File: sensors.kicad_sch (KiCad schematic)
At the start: 21 parts, among them U11 BMP280, U12 MMC5633NJL, U16 Si7020-A20, U17 TXB0108PW, U3 IIM-42652, U4 QMI8610, U9 PCA9306DC1

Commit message: MOS管修改为GSD, 添加芯片附近滤波电容、上拉电阻等，调整模块间布局，改正AHT20封装，电解电容替换成1210 MLCC
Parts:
- removed U16: Si7020-A20, Package_DFN_QFN:DFN-6-1EP_3x3mm_P1mm_EP1.5x2.4mm, symbol Sensor_Humidity:Si7020-A20
- added C33: 2.2uf, Capacitor_SMD:C_0603_1608Metric, symbol Device:C_Small
- added C34: 10uf, Capacitor_SMD:C_0603_1608Metric, symbol Device:C
- added C35: 0.1uf, Capacitor_SMD:C_0402_1005Metric, symbol Device:C_Small
- added R32: R, Resistor_SMD:R_0603_1608Metric, symbol Device:R
- added U5: AHT20, Library:DFN-6_3x3mm_P1.0mm_AHT2x_AHT30, symbol New_Library:AHT2x
- C10: value C_Small -> 10nF
- C11, C12, C15, C17, C18, C20, C21: value C_Small -> 100nF
- C19, C9: value C_Small -> 0.1uf
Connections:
- net +1V8: now also C33.2, C35.2
- net +3.3V: now also R32.1
- net GND: now also C33.1, C34.2, C35.1, U5.5 (GND)
- net SCL: now also U5.3 (SCL)
- net SDA: now also U5.4 (SDA)
- new net: U5.1 (NC), U5.6 (NC)
- new net: C34.1, R32.2, U5.2 (VDD)
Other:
- moved on the sheet: C10

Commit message: 连接大多数布线，做一些调整，添加覆铜
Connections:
- net +1V8: now also U11.2 (CSB)
- net SCL1V8: now also U11.4 (SCK)
- net SDA1V8: now also U11.3 (SDI)
- net SPISen_CS_QMI_1V8: now also U17.4 (A3); no longer U17.1 (A1)
- net SPISen_CS_TDK_1V8: now also U17.8 (A7); no longer U17.3 (A2)
- net SPISen_MISO_1V8: now also U17.6 (A5); no longer U11.5 (SDO), U17.7 (A6)
- net SPISen_MOSI_1V8: now also U17.7 (A6); no longer U11.3 (SDI), U17.5 (A4)
- net SPISen_SCLK_1V8: now also U17.5 (A4); no longer U11.4 (SCK), U17.6 (A5)
- net TDK_INT2_1V8: now also U17.9 (A8); no longer U17.8 (A7)
- net TDK_INT2_3V3: now also U17.12 (B8); no longer U17.13 (B7)
- removed net SPISen_CS_BMP_1V8: U11.2 (CSB), U17.4 (A3)
- net SPISen_CS_BMP_3V3 renamed CS_QMI_3V3
- net SPISen_CS_QMI_3V3: no longer names the net of U17.20 (B1)
- net SPISen_CS_TDK_3V3: no longer names the net of U17.18 (B2)
- net SPISen_MISO_3V3 renamed MOSI_3V3
- net SPISen_MOSI_3V3 renamed SCLK_3V3
- net SPISen_SCLK_3V3 renamed MISO_3V3
- new net CS_TDK_3V3: U17.13 (B7)
- no-connect marks 2 -> 3
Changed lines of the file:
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@@
+	)
+	(junction
+		(at 158.75 104.14)
+		(diameter 0)
+		(color 0 0 0 0)
 	)
 	(junction
@@
 	)
 	(no_connect
+		(at 148.59 114.3)
+	)
+	(no_connect
 		(at 146.05 44.45)
 	)
@@
 	(wire
 		(pts
-			(xy 147.32 116.84) (xy 148.59 116.84)
-		)
-		(stroke
-			(width 0)
-			(type default)
-		)
-	)
-	(wire
-		(pts
 			(xy 243.84 76.2) (xy 245.11 76.2)
 		)
@@
 	(wire
 		(pts
-			(xy 147.32 114.3) (xy 148.59 114.3)
-		)
-		(stroke
-			(width 0)
-			(type default)
-		)
-	)
-	(wire
-		(pts
 			(xy 115.57 113.03) (xy 115.57 116.84)
 		)
@@
 	(wire
 		(pts
+			(xy 158.75 116.84) (xy 158.75 104.14)
+		)
+		(stroke
+			(width 0)
+			(type default)
+		)
+	)
+	(wire
+		(pts
 			(xy 166.37 115.57) (xy 166.37 123.19)
 		)
@@
 	(wire
 		(pts
+			(xy 148.59 116.84) (xy 158.75 116.84)
+		)
+		(stroke
+			(width 0)
+			(type default)
+		)
+	)
+	(wire
+		(pts
 			(xy 220.98 78.74) (xy 223.52 78.74)
 		)
@@
 		)
 	)
-	(label "SPISen_MOSI_3V3"
-		(at 245.11 68.58 0)
-		(fields_autoplaced yes)
-		(effects
-			(font
-				(size 1.27 1.27)
-			)
-			(justify left bottom)
+	(label "SDA1V8"
+		(at 147.32 111.76 180)
+		(fields_autoplaced yes)
+		(effects
+			(font
+				(size 1.27 1.27)
+			)
+			(justify right bottom)
 		)
 	)
 	(label "SPISen_MOSI_1V8"
-		(at 220.98 68.58 180)
+		(at 220.98 73.66 180)
 		(fields_autoplaced yes)
 		(effects
@@
 		)
 	)
-	(label "SPISen_CS_BMP_3V3"
-		(at 245.11 66.04 0)
-		(fields_autoplaced yes)
-		(effects
-			(font
-				(size 1.27 1.27)
-			)
-			(justify left bottom)
-		)
-	)
-	(label "SPISen_MOSI_1V8"
-		(at 147.32 111.76 180)
-		(fields_autoplaced yes)
-		(effects
-			(font
-				(size 1.27 1.27)
-			)
-			(justify right bottom)
-		)
-	)
 	(label "SDA1V8"
 		(at 46.99 80.01 180)
@@
 		)
 	)
-	(label "SPISen_CS_QMI_1V8"
-		(at 220.98 60.96 180)
-		(fields_autoplaced yes)
-		(effects
-			(font
-				(size 1.27 1.27)
-			)
-			(justify right bottom)
-		)
-	)
 	(label "QMI_INT2"
 		(at 172.72 40.64 0)
@@
 		)
 	)
-	(label "SPISen_CS_QMI_3V3"
-		(at 245.11 60.96 0)
-		(fields_autoplaced yes)
-		(effects
-			(font
-				(size 1.27 1.27)
-			)
-			(justify left bottom)
+	(label "SPISen_CS_TDK_1V8"
+		(at 220.98 76.2 180)
+		(fields_autoplaced yes)
+		(effects
+			(font
+				(size 1.27 1.27)
+			)
+			(justify right bottom)
 		)
 	)
@@
 		)
 	)
+	(label "SPISen_SCLK_1V8"
+		(at 220.98 68.58 180)
+		(fields_autoplaced yes)
+		(effects
+			(font
+				(size 1.27 1.27)
+			)
+			(justify right bottom)
+		)
+	)
 	(label "SPISen_MISO_1V8"
-		(at 147.32 114.3 180)
+		(at 220.98 71.12 180)
 		(fields_autoplaced yes)
 		(effects
@@
 		)
 	)
-	(label "SPISen_CS_TDK_1V8"
-		(at 220.98 63.5 180)
-		(fields_autoplaced yes)
-		(effects
-			(font
-				(size 1.27 1.27)
-			)
-			(justify right bottom)
-		)
-	)
 	(label "SPISen_MOSI_1V8"
 		(at 172.72 45.72 0)
@@
 		)
 	)
+	(label "TDK_INT2_1V8"
+		(at 220.98 78.74 180)
+		(fields_autoplaced yes)
+		(effects
+			(font
+				(size 1.27 1.27)
+			)
+			(justify right bottom)
+		)
+	)
 	(label "SCL1V8"
 		(at 46.99 77.47 180)
@@
 		)
 	)
-	(label "TDK_INT2_1V8"
-		(at 220.98 76.2 180)
-		(fields_autoplaced yes)
-		(effects
-			(font
-				(size 1.27 1.27)
-			)
-			(justify right bottom)
-		)
-	)
-	(label "SPISen_CS_BMP_1V8"
+	(label "SPISen_CS_QMI_1V8"
 		(at 220.98 66.04 180)
-		(fields_autoplaced yes)
-		(effects
-			(font
-				(size 1.27 1.27)
-			)
-			(justify right bottom)
-		)
-	)
-	(label "TDK_INT2_3V3"
-		(at 245.11 76.2 0)
-		(fields_autoplaced yes)
-		(effects
-			(font
-				(size 1.27 1.27)
-			)
-			(justify left bottom)
-		)
-	)
-	(label "SPISen_CS_BMP_1V8"
-		(at 147.32 116.84 180)
 		(fields_autoplaced yes)
 		(effects
@@
 		)
 	)
-	(label "SPISen_MISO_3V3"
-		(at 245.11 73.66 0)
-		(fields_autoplaced yes)
-		(effects
-			(font
-				(size 1.27 1.27)
-			)
-			(justify left bottom)
-		)
-	)
-	(label "SPISen_SCLK_1V8"
-		(at 220.98 71.12 180)
-		(fields_autoplaced yes)
-		(effects
-			(font
-				(size 1.27 1.27)
-			)
-			(justify right bottom)
-		)
-	)
 	(label "TDK_INT1"
 		(at 128.27 43.18 0)
@@
 		)
 	)
-	(label "SPISen_CS_TDK_3V3"
-		(at 245.11 63.5 0)
-		(fields_autoplaced yes)
-		(effects
-			(font
-				(size 1.27 1.27)
-			)
-			(justify left bottom)
-		)
-	)
-	(label "SPISen_MISO_1V8"
-		(at 220.98 73.66 180)
-		(fields_autoplaced yes)
-		(effects
-			(font
-				(size 1.27 1.27)
-			)
-			(justify right bottom)
-		)
-	)
 	(label "SDA"
 		(at 215.9 114.3 180)
@@
 	)
 	(label "SPISen_SCLK_1V8"
-		(at 147.32 109.22 180)
-		(fields_autoplaced yes)
-		(effects
-			(font
-				(size 1.27 1.27)
-			)
-			(justify right bottom)
-		)
-	)
-	(label "SPISen_SCLK_1V8"
 		(at 80.01 43.18 180)
 		(fields_autoplaced yes)
@@
 		)
 	)
-	(label "SPISen_SCLK_3V3"
-		(at 245.11 71.12 0)
-		(fields_autoplaced yes)
-		(effects
-			(font
-				(size 1.27 1.27)
-			)
-			(justify left bottom)
+	(label "SCL1V8"
+		(at 147.32 109.22 180)
+		(fields_autoplaced yes)
+		(effects
+			(font
+				(size 1.27 1.27)
+			)
+			(justify right bottom)
 		)
 	)
@@
 		(fields_autoplaced yes)
 		(effects
+			(font
+				(size 1.27 1.27)
+			)
+			(justify left)
+		)
+	)
+	(hierarchical_label "MISO_3V3"
+		(shape output)
+		(at 245.11 71.12 0)
+		(fields_autoplaced yes)
+		(effects
+			(font
+				(size 1.27 1.27)
+			)
+			(justify left)
+		)
+	)
+	(hierarchical_label "MOSI_3V3"
+		(shape input)
+		(at 245.11 73.66 0)
+		(fields_autoplaced yes)
+		(effects
+			(font
+				(size 1.27 1.27)
+			)
+			(justify left)
+		)
+	)
+	(hierarchical_label "CS_TDK_3V3"
+		(shape input)
+		(at 245.11 76.2 0)
+		(fields_autoplaced yes)
+		(effects
+			(font
+				(size 1.27 1.27)
+			)
+			(justify left)
+		)
+	)
+	(hierarchical_label "TDK_INT2_3V3"
+		(shape bidirectional)
+		(at 245.11 78.74 0)
+		(fields_autoplaced yes)
+		(effects
+			(font
+				(size 1.27 1.27)
+			)
+			(justify left)
+		)
+	)
+	(hierarchical_label "CS_QMI_3V3"
+		(shape input)
+		(at 245.11 66.04 0)
+		(fields_autoplaced yes)
+		(effects
+			(font
+				(size 1.27 1.27)
+			)
+			(justify left)
+		)
+	)
+	(hierarchical_label "SCLK_3V3"
+		(shape input)
+		(at 245.11 68.58 0)
+		(fields_autoplaced yes)
+		(effects

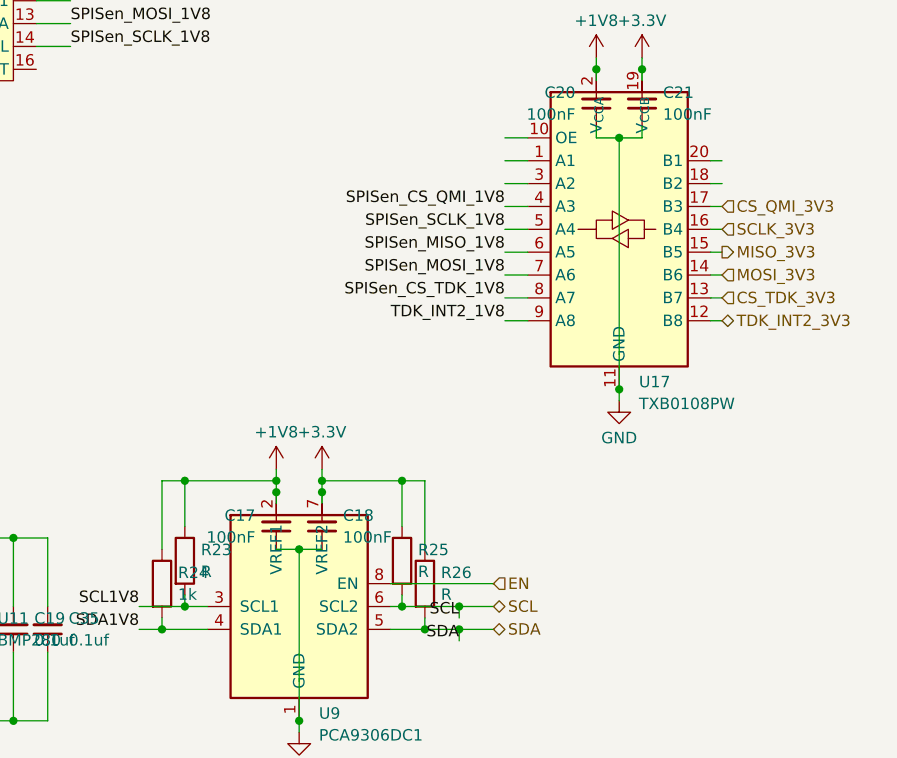
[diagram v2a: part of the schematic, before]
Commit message: 移除第二个74HC595，SGM2033-1.8改成一直开启，按PCA9306数据手册修改供电
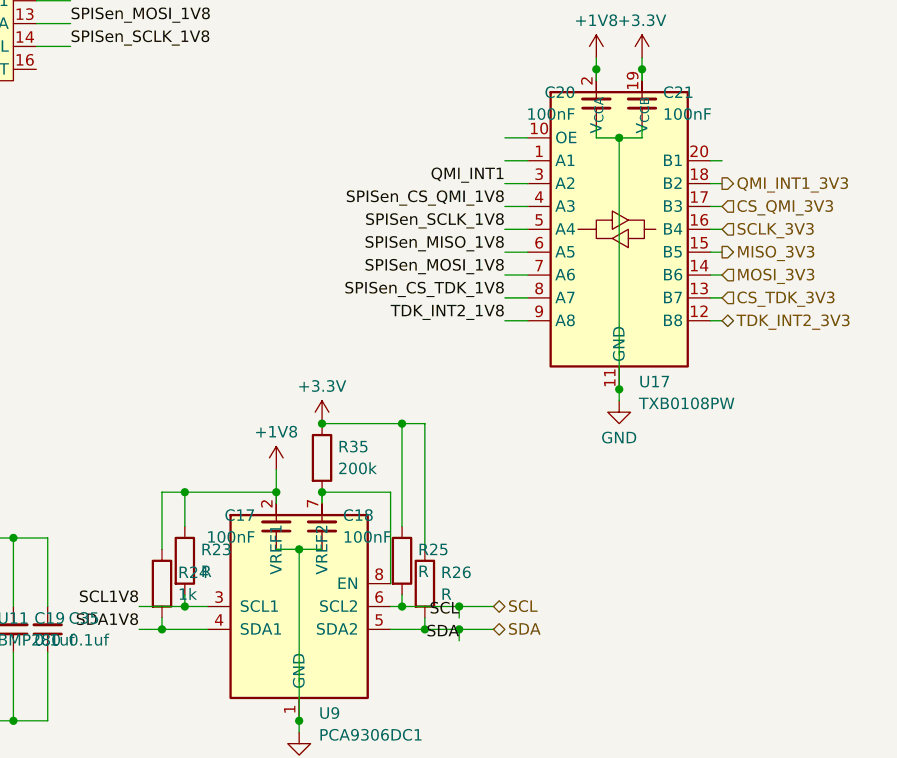
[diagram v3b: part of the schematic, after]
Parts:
- added R35: 200k, Resistor_SMD:R_0402_1005Metric, symbol Device:R
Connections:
- net +3.3V: now also R35.1; no longer C18.2, U9.7 (VREF2)
- net QMI_INT1: now also U17.3 (A2)
- net QMI_INT1_3V3: now reaches U17.18 (B2)
- net EN: no longer names the net of U9.8 (EN)
- net EN: now also C18.2, U9.7 (VREF2), R35.2
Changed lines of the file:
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@@
 	)
 	(junction
-		(at 185.42 96.52)
+		(at 209.55 90.17)
 		(diameter 0)
 		(color 0 0 0 0)
@@
 	)
 	(junction
-		(at 195.58 96.52)
-		(diameter 0)
-		(color 0 0 0 0)
-	)
-	(junction
 		(at 97.79 24.13)
 		(diameter 0)
@@
 	)
 	(junction
-		(at 200.66 96.52)
-		(diameter 0)
-		(color 0 0 0 0)
-	)
-	(junction
 		(at 212.09 113.03)
 		(diameter 0)
@@
 	)
 	(junction
+		(at 185.42 97.79)
+		(diameter 0)
+		(color 0 0 0 0)
+	)
+	(junction
 		(at 161.29 102.87)
 		(diameter 0)
@@
 	)
 	(junction
+		(at 200.66 90.17)
+		(diameter 0)
+		(color 0 0 0 0)
+	)
+	(junction
 		(at 161.29 123.19)
 		(diameter 0)
@@
 	)
 	(junction
-		(at 209.55 96.52)
-		(diameter 0)
-		(color 0 0 0 0)
-	)
-	(junction
 		(at 215.9 110.49)
 		(diameter 0)
@@
 	(wire
 		(pts
-			(xy 195.58 97.79) (xy 195.58 96.52)
-		)
-		(stroke
-			(width 0)
-			(type default)
-		)
-	)
-	(wire
-		(pts
 			(xy 104.14 29.21) (xy 104.14 30.48)
 		)
@@
 	(wire
 		(pts
-			(xy 195.58 95.25) (xy 195.58 96.52)
+			(xy 200.66 97.79) (xy 200.66 99.06)
 		)
 		(stroke
@@
 	(wire
 		(pts
-			(xy 212.09 96.52) (xy 209.55 96.52)
+			(xy 212.09 90.17) (xy 209.55 90.17)
 		)
 		(stroke
@@
 	(wire
 		(pts
-			(xy 200.66 96.52) (xy 209.55 96.52)
+			(xy 200.66 90.17) (xy 209.55 90.17)
 		)
 		(stroke
@@
 	(wire
 		(pts
-			(xy 182.88 96.52) (xy 185.42 96.52)
+			(xy 182.88 97.79) (xy 185.42 97.79)
 		)
 		(stroke
@@
 	(wire
 		(pts
-			(xy 170.18 110.49) (xy 170.18 102.87)
+			(xy 208.28 97.79) (xy 208.28 107.95)
 		)
 		(stroke
@@
 	(wire
 		(pts
-			(xy 115.57 113.03) (xy 115.57 116.84)
+			(xy 195.58 95.25) (xy 195.58 97.79)
 		)
 		(stroke
@@
 	(wire
 		(pts
-			(xy 71.12 72.39) (xy 58.42 72.39)
+			(xy 170.18 110.49) (xy 170.18 102.87)
 		)
 		(stroke
@@
 	(wire
 		(pts
-			(xy 158.75 104.14) (xy 158.75 102.87)
+			(xy 115.57 113.03) (xy 115.57 116.84)
 		)
 		(stroke
@@
 	(wire
 		(pts
-			(xy 209.55 101.6) (xy 209.55 96.52)
+			(xy 71.12 72.39) (xy 58.42 72.39)
 		)
 		(stroke
@@
 	(wire
 		(pts
-			(xy 166.37 110.49) (xy 166.37 102.87)
+			(xy 158.75 104.14) (xy 158.75 102.87)
 		)
 		(stroke
@@
 	(wire
 		(pts
-			(xy 115.57 101.6) (xy 107.95 101.6)
+			(xy 209.55 90.17) (xy 209.55 101.6)
 		)
 		(stroke
@@
 	(wire
 		(pts
-			(xy 158.75 102.87) (xy 160.02 102.87)
+			(xy 166.37 110.49) (xy 166.37 102.87)
 		)
 		(stroke
@@
 	(wire
 		(pts
-			(xy 198.12 123.19) (xy 198.12 124.46)
+			(xy 115.57 101.6) (xy 107.95 101.6)
 		)
 		(stroke
@@
 	(wire
 		(pts
-			(xy 200.66 95.25) (xy 200.66 96.52)
+			(xy 158.75 102.87) (xy 160.02 102.87)
 		)
 		(stroke
@@
 	(wire
 		(pts
-			(xy 46.99 80.01) (xy 48.26 80.01)
+			(xy 198.12 123.19) (xy 198.12 124.46)
 		)
 		(stroke
@@
 	(wire
 		(pts
-			(xy 212.09 104.14) (xy 212.09 96.52)
+			(xy 46.99 80.01) (xy 48.26 80.01)
 		)
 		(stroke
@@
 	(wire
 		(pts
-			(xy 200.66 99.06) (xy 200.66 97.79)
+			(xy 212.09 90.17) (xy 212.09 104.14)
 		)
 		(stroke
@@
 	(wire
 		(pts
-			(xy 200.66 96.52) (xy 200.66 97.79)
-		)
-		(stroke
-			(width 0)
-			(type default)
-		)
-	)
-	(wire
-		(pts
 			(xy 212.09 111.76) (xy 212.09 113.03)
 		)
@@
 	(wire
 		(pts
-			(xy 182.88 104.14) (xy 182.88 96.52)
+			(xy 182.88 104.14) (xy 182.88 97.79)
 		)
 		(stroke
@@
 	(wire
 		(pts
-			(xy 185.42 101.6) (xy 185.42 96.52)
+			(xy 185.42 101.6) (xy 185.42 97.79)
 		)
 		(stroke
@@
 	(wire
 		(pts
-			(xy 185.42 96.52) (xy 195.58 96.52)
+			(xy 185.42 97.79) (xy 195.58 97.79)
 		)
 		(stroke
@@
 	(wire
 		(pts
-			(xy 208.28 107.95) (xy 219.71 107.95)
+			(xy 200.66 97.79) (xy 208.28 97.79)
 		)
 		(stroke
@@
 		)
 	)
+	(label "QMI_INT1"
+		(at 220.98 63.5 180)
+		(fields_autoplaced yes)
+		(effects
+			(font
+				(size 1.27 1.27)
+			)
+			(justify right bottom)
+		)
+	)
 	(label "TDK_INT2_1V8"
 		(at 220.98 78.74 180)
@@
 		)
 	)
-	(hierarchical_label "EN"
-		(shape input)
-		(at 219.71 107.95 0)
+	(hierarchical_label "QMI_INT1_3V3"
+		(shape output)
+		(at 245.11 63.5 0)
 		(fields_autoplaced yes)
 		(effects
@@
 	)
 	(symbol
+		(lib_id "Device:R")
+		(at 200.66 93.98 0)
+		(unit 1)
+		(exclude_from_sim no)
+		(in_bom yes)
+		(on_board yes)
+		(dnp no)
+		(fields_autoplaced yes)
+		(property "Reference" "R35"
+			(at 202.438 92.7678 0)
+			(effects
+				(font
+					(size 1.27 1.27)
+				)
+				(justify left)
+			)
+		)
+		(property "Value" "200k"
+			(at 202.438 95.1921 0)
+			(effects
+				(font
+					(size 1.27 1.27)
+				)
+				(justify left)
+			)
+		)
+		(property "Footprint" "Resistor_SMD:R_0402_1005Metric"
+			(at 198.882 93.98 90)
+			(effects
+				(font
+					(size 1.27 1.27)
+				)
+				(hide yes)
+			)
+		)
+		(property "Datasheet" "~"
+			(at 200.66 93.98 0)
+			(effects
+				(font
+					(size 1.27 1.27)
+				)
+				(hide yes)
+			)
+		)
+		(property "Description" "Resistor"
+			(at 200.66 93.98 0)
+			(effects
+				(font
+					(size 1.27 1.27)
+				)
+				(hide yes)
+			)
+		)
+		(property "Sim.Type" ""
+			(at 200.66 93.98 0)
+			(effects
+				(font
+					(size 1.27 1.27)
+				)
+				(hide yes)
+			)
+		)
+		(pin "2"
+		)
+		(pin "1"
+		)
+		(instances
+			(project "bicycle_board"
+				(path "/a369956d-4c9f-46c3-810f-e3e9616ab1a2/490df38e-4ea0-4947-96c5-2fbeb0d565d2"
+					(reference "R35")
+					(unit 1)
+				)
+			)
+		)
+	)
+	(symbol
 		(lib_id "power:GND")
 		(at 233.68 87.63 0)
@@
 	(symbol
 		(lib_id "power:+3.3V")
-		(at 200.66 95.25 0)
+		(at 200.66 90.17 0)
 		(unit 1)
 		(exclude_from_sim no)
@@
 		(fields_autoplaced yes)
 		(property "Reference" "#PWR037"
-			(at 200.66 99.06 0)
+			(at 200.66 93.98 0)
 			(effects
 				(font
@@
 		)
 		(property "Value" "+3.3V"
-			(at 200.66 91.1169 0)
+			(at 200.66 86.0369 0)
 			(effects
 				(font
@@
 		)
 		(property "Footprint" ""
-			(at 200.66 95.25 0)
+			(at 200.66 90.17 0)
 			(effects
 				(font
@@
 		)
 		(property "Datasheet" ""
-			(at 200.66 95.25 0)
+			(at 200.66 90.17 0)
 			(effects
 				(font
@@
 		)
 		(property "Description" "Power symbol creates a global label with name \"+3.3V\""
-			(at 200.66 95.25 0)
+			(at 200.66 90.17 0)
 			(effects
 				(font

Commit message: 工程中修改为正确芯片型号QMC6308,ICM-42688-P，按数据手册更新供电滤波电容值
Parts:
- C15: value 100nF -> 2.2uF
- R32: value R -> 330
- U12: value MMC5633NJL -> QMC6308
- U3: value IIM-42652 -> ICM-42688-P
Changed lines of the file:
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@@
 			)
 		)
-		(property "Value" "100nF"
+		(property "Value" "2.2uF"
 			(at 73.4441 81.2157 0)
 			(effects
@@
 			)
 		)
-		(property "Value" "IIM-42652"
+		(property "Value" "ICM-42688-P"
 			(at 106.3341 57.4844 0)
 			(effects
@@
 			)
 		)
-		(property "Datasheet" "https://invensense.tdk.com/wp-content/uploads/2021/01/ds-000440_iim-42652-datasheet.pdf"
+		(property "Datasheet" "https://product.tdk.com.cn/system/files/dam/doc/product/sensor/mortion-inertial/imu/data_sheet/ds-000347-icm-42688-p-v1.6.pdf"
 			(at 104.14 48.26 0)
 			(effects
@@
 			)
 		)
-		(property "Value" "R"
+		(property "Value" "330"
 			(at 109.728 97.7321 0)
 			(effects
@@
 			)
 		)
-		(property "Value" "MMC5633NJL"
+		(property "Value" "QMC6308"
 			(at 66.802 81.2221 0)
 			(effects
@@
 			)
 		)
-		(property "Datasheet" "http://www.memsic.com/uploadfiles/2020/08/20200827165106864.pdf"
+		(property "Datasheet" "https://www.qstcorp.com/upload/pdf/202202/13-52-15%20QMC6308%20Datasheet%20Rev.%20F(1).pdf"
 			(at 55.88 80.01 0)
 			(effects
@@
 			)
 		)
-		(property "Description" "3-axis AMR Magnetometer, 30 G, I2C & I3C  Interface, 2mG RMS, WLP-4"
+		(property "Description" "3-axis AMR Magnetometer, 30 G, I2C Interface, 2mG RMS, WLP-4"
 			(at 58.42 80.01 0)
 			(effects

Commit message: 添加第二个磁力计QMC7983
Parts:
- added C59: 4.7uF, Capacitor_SMD:C_0603_1608Metric, symbol Device:C
- added C60: 100nF, Capacitor_SMD:C_0402_1005Metric, symbol Device:C_Small
- added U19: QMC7983, Library:WLP-8_1.2x1.2mm_Layout3x3_P0.4mm_Pad0.24mm, symbol New_Library:QMC7983
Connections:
- net +1V8: now also C60.1, U19.C1 (DVDD)
- net +3.3V: now also C59.1, U19.A1 (AVDD), U19.A2 (ADDR)
- net GND: now also C59.2, C60.2, U19.B1 (GND)
- net SCL1V8: now also U19.B3 (SCL)
- net SDA1V8: now also U19.C3 (SDA)

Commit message: 修复一些ERC错误
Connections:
- no-connect marks 3 -> 6
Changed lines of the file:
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@@
+	)
+	(no_connect
+		(at 220.98 60.96)
 	)
 	(no_connect
 		(at 146.05 41.91)
+	)
+	(no_connect
+		(at 245.11 60.96)
 	)
 	(no_connect
@@
 		(at 146.05 44.45)
 	)
+	(no_connect
+		(at 220.98 58.42)
+	)
 	(wire
